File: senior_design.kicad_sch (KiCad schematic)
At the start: 0 parts

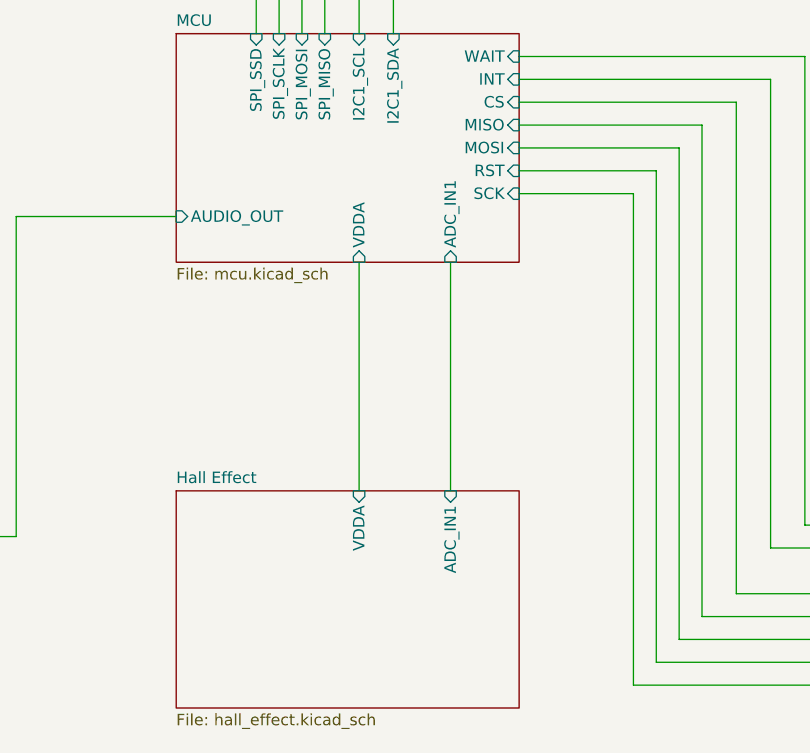
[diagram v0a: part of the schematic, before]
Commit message: added HE2 and expanded VDDA plane
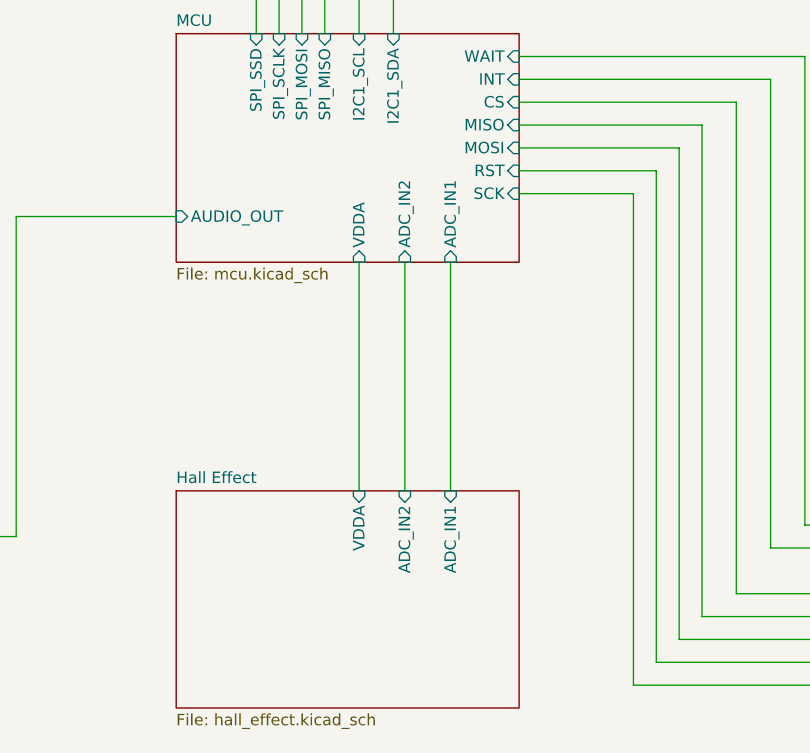
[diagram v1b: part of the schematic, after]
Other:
- sheet Hall Effect ports: added ADC_IN2; removed none
- sheet MCU ports: added ADC_IN2; removed none
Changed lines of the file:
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@@
+	(wire
+		(pts
+			(xy 152.4 76.2) (xy 152.4 101.6)
+		)
+		(stroke
+			(width 0)
+			(type default)
+		)
+	)
 	(wire
 		(pts
@@
 			)
 		)
+		(pin "ADC_IN2" input
+			(at 152.4 76.2 270)
+			(effects
+				(font
+					(size 1.27 1.27)
+				)
+				(justify left)
+			)
+		)
 		(instances
 			(project "senior_design"
@@
 			(effects
 				(font
+					(size 1.27 1.27)
+				)
+				(justify right)
+			)
+		)
+		(pin "ADC_IN2" input
+			(at 152.4 101.6 90)
+			(effects
+				(font

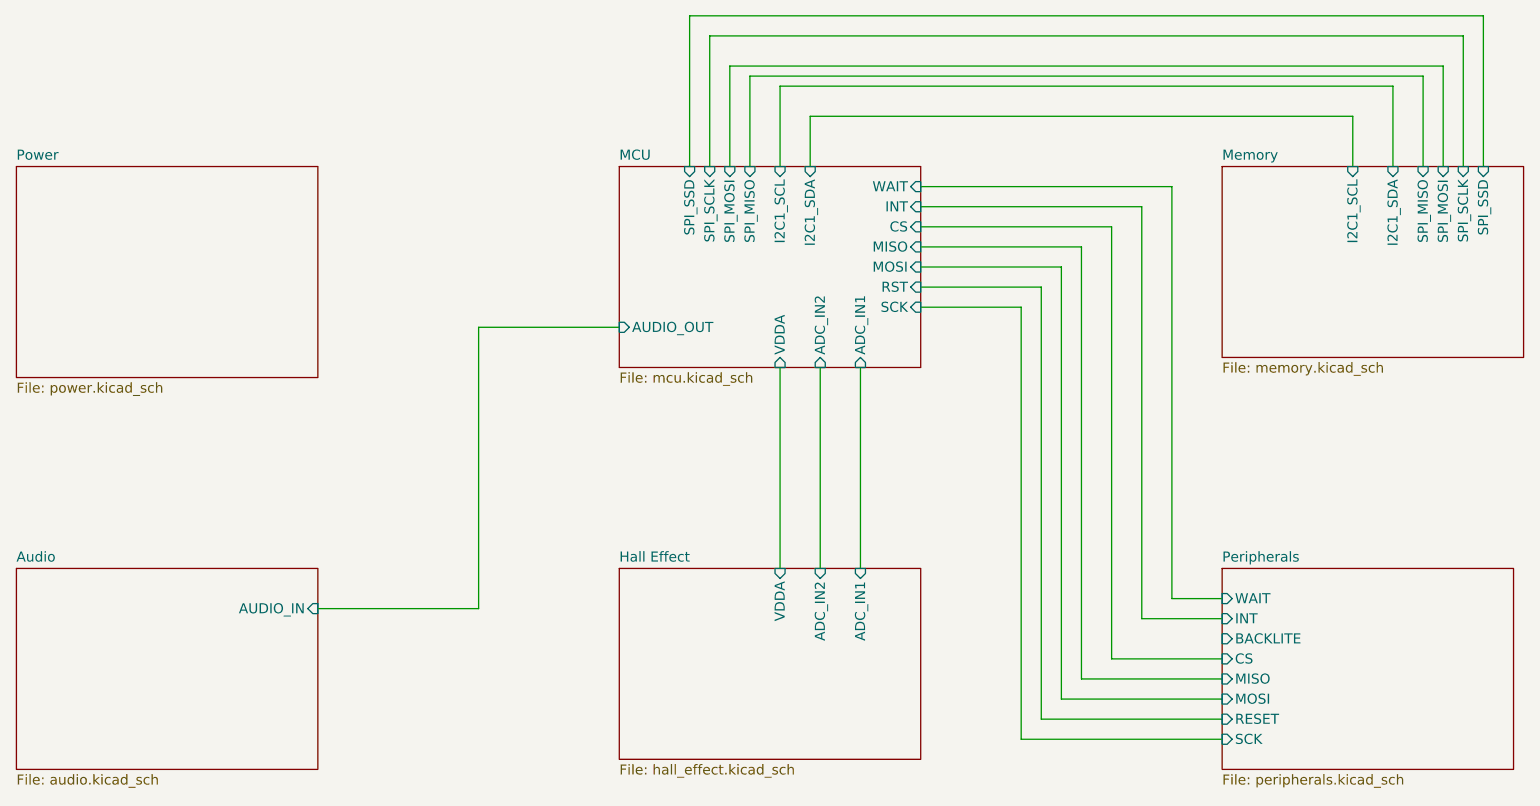
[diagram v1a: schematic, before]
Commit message: Fixed labels and added datasheets
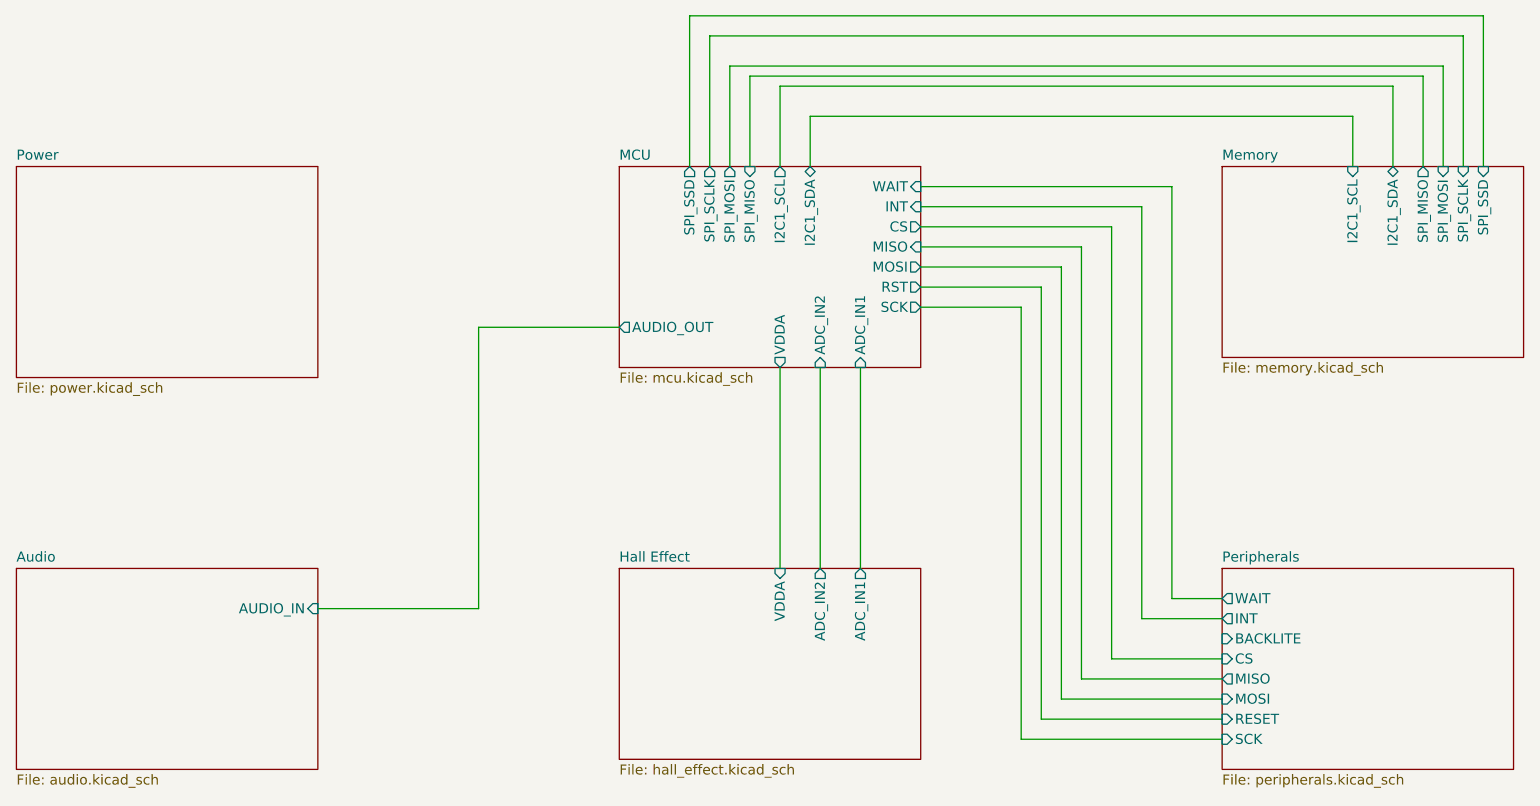
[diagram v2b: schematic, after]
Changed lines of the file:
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@@
 			)
 		)
-		(pin "CS" input
+		(pin "CS" output
 			(at 165.1 58.42 0)
 			(effects
@@
 			)
 		)
-		(pin "MOSI" input
+		(pin "MOSI" output
 			(at 165.1 63.5 0)
 			(effects
@@
 			)
 		)
-		(pin "RST" input
+		(pin "RST" output
 			(at 165.1 66.04 0)
 			(effects
@@
 			)
 		)
-		(pin "SCK" input
+		(pin "SCK" output
 			(at 165.1 68.58 0)
 			(effects
@@
 			)
 		)
-		(pin "I2C1_SCL" input
+		(pin "I2C1_SCL" output
 			(at 147.32 50.8 90)
 			(effects
@@
 			)
 		)
-		(pin "I2C1_SDA" input
+		(pin "I2C1_SDA" bidirectional
 			(at 151.13 50.8 90)
 			(effects
@@
 			)
 		)
-		(pin "SPI_MOSI" input
+		(pin "SPI_MOSI" output
 			(at 140.97 50.8 90)
 			(effects
@@
 			)
 		)
-		(pin "SPI_SCLK" input
+		(pin "SPI_SCLK" output
 			(at 138.43 50.8 90)
 			(effects
@@
 			)
 		)
-		(pin "SPI_SSD" input
+		(pin "SPI_SSD" output
 			(at 135.89 50.8 90)
 			(effects
@@
 			)
 		)
-		(pin "AUDIO_OUT" input
+		(pin "AUDIO_OUT" output
 			(at 127 71.12 180)
 			(effects
@@
 			)
 		)
-		(pin "VDDA" input
+		(pin "VDDA" output
 			(at 147.32 76.2 270)
 			(effects
@@
 			)
 		)
-		(pin "I2C1_SDA" input
+		(pin "I2C1_SDA" bidirectional
 			(at 224.79 50.8 90)
 			(effects
@@
 			)
 		)
-		(pin "SPI_MISO" input
+		(pin "SPI_MISO" output
 			(at 228.6 50.8 90)
 			(effects
@@
 			)
 		)
-		(pin "ADC_IN1" input
+		(pin "ADC_IN1" output
 			(at 157.48 101.6 90)
 			(effects
@@
 			)
 		)
-		(pin "ADC_IN2" input
+		(pin "ADC_IN2" output
 			(at 152.4 101.6 90)
 			(effects
@@
 			)
 		)
-		(pin "INT" input
+		(pin "INT" output
 			(at 203.2 107.95 180)
 			(effects
@@
 			)
 		)
-		(pin "MISO" input
+		(pin "MISO" output
 			(at 203.2 115.57 180)
 			(effects
@@
 			)
 		)
-		(pin "WAIT" input
+		(pin "WAIT" output
 			(at 203.2 105.41 180)
 			(effects
